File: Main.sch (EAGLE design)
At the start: 41 parts, among them IC1 LM35CZ, Q1 IRLZ44N, T1 2N3904, U1 PIC18F45K22-I/P, X1 22-23-2021

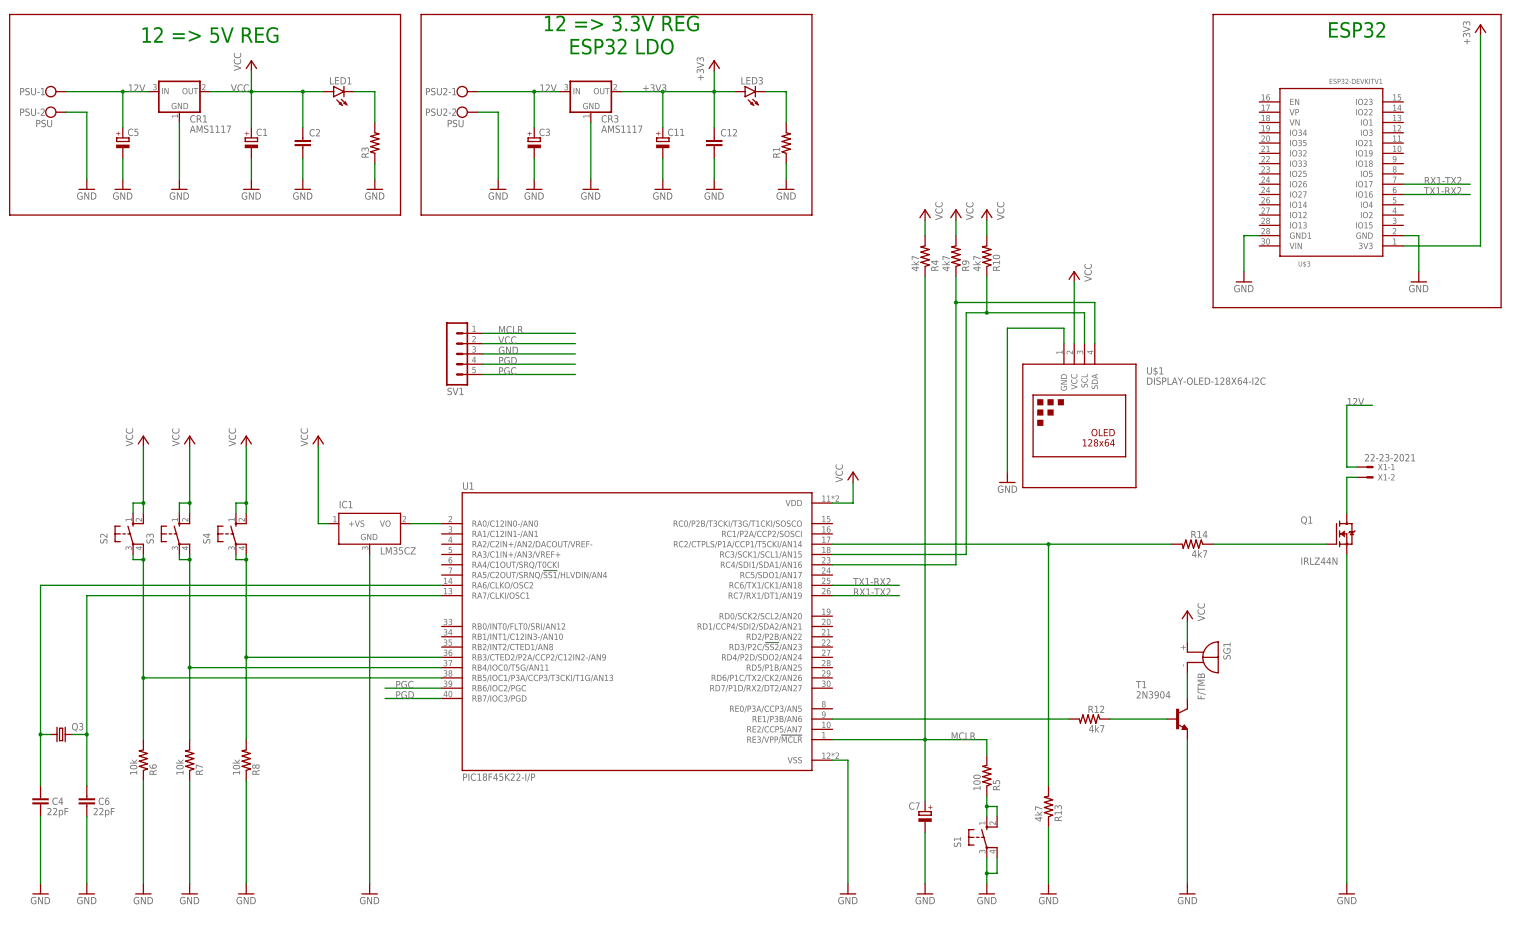
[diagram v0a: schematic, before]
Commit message: Schematic Rearranged
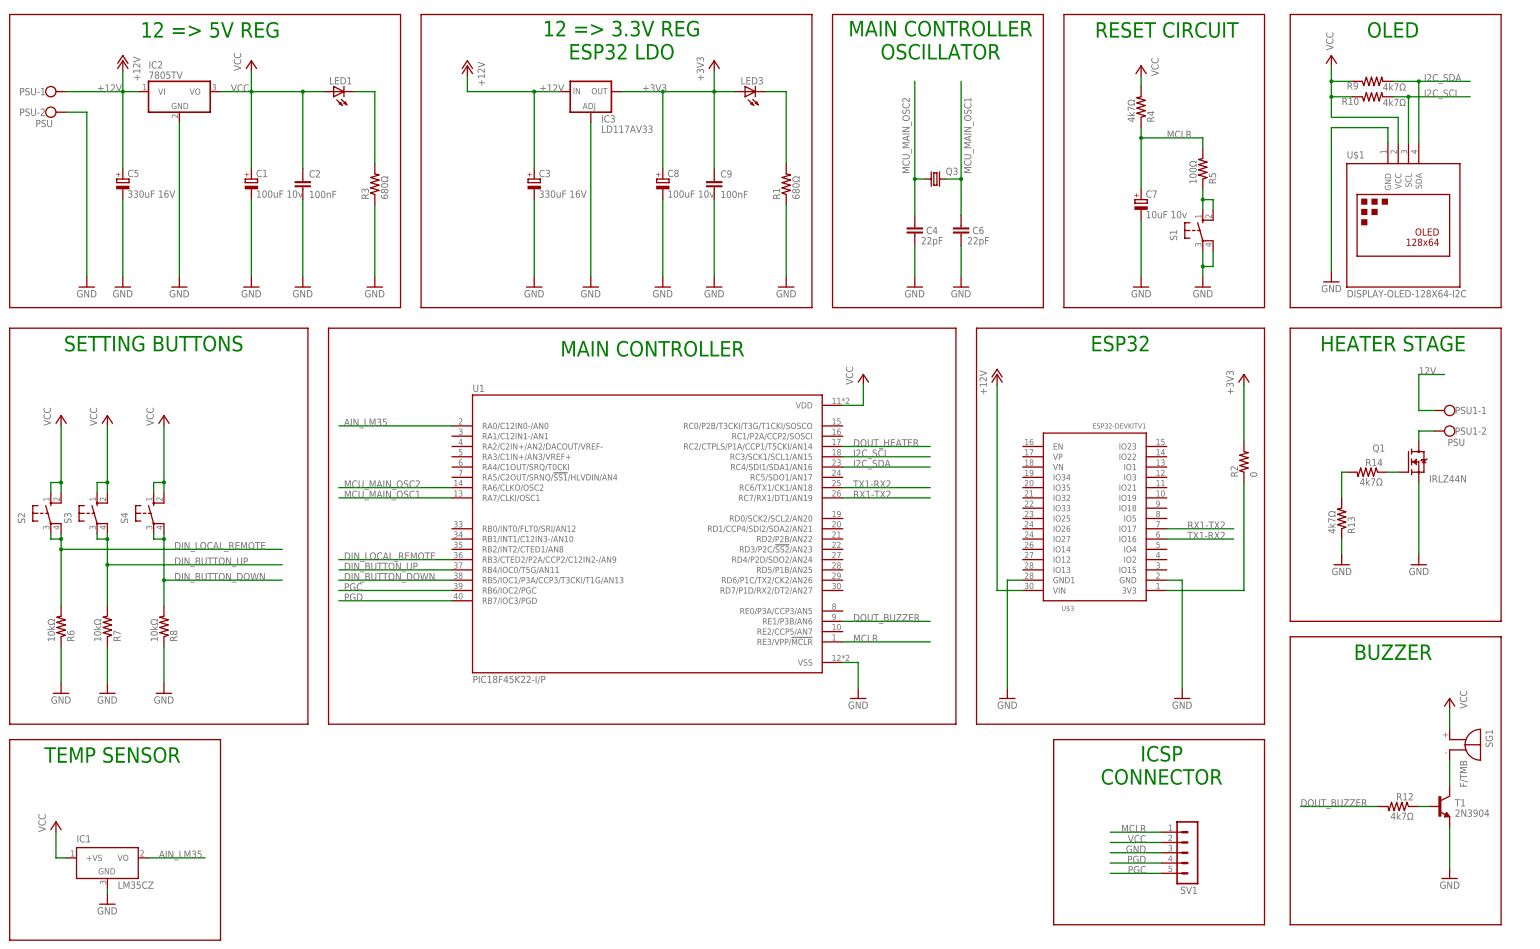
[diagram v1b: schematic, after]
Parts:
- removed C11: (no value), resistor:CPOL-EU153CLV-0505
- removed C12: (no value), resistor:C-EUC0805
- removed CR1, CR3: AMS1117, AMS1117:AMS1117
- removed PSU2: PSU, con-wago-500:W237-102
- removed X1: 22-23-2021, con-molex:22-23-2021
- added C8: 100uF 10v, resistor:CPOL-EUE2-5
- added C9: 100nF, resistor:C-EU025-060X050
- added IC2: 7805TV, linear:7805TV
- added IC3: LD117AV33, v-reg:LD117AV33
- added PSU1: PSU, con-wago-500:W237-102
- added R2: 0, resistor:R-US_0204/7
- C1: value (none) -> 100uF 10v; device resistor:CPOL-EU153CLV-0505 -> resistor:CPOL-EUE2-5
- C2: value (none) -> 100nF; device resistor:C-EUC0805 -> resistor:C-EU025-060X050
- C3, C5: value (none) -> 330uF 16V; device resistor:CPOL-EU153CLV-0505 -> resistor:CPOL-EUE2-5
- C4, C6: device resistor:C-EUC0805 -> resistor:C-EU025-024X044
- C7: value (none) -> 10uF 10v; device resistor:CPOL-EU153CLV-0505 -> resistor:CPOL-EUE2-5
- LED1, LED3: device led:LEDSML0805 -> led:LED5MM
- R1, R3: value (none) -> 680Ω
- R10, R12, R13, R14, R4, R9: value 4k7 -> 4k7Ω
- R5: value 100 -> 100Ω
- R6, R7, R8: value 10k -> 10kΩ
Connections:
- net MCU_XI2 renamed MCU_MAIN_OSC2
- net MCU_XO2 renamed MCU_MAIN_OSC1
- net N$19 renamed DOUT_BUZZER
- net N$20 renamed AIN_LM35
- net N$7 renamed DIN_BUTTON_UP
- removed net N$17: R10.1, U$1.SCL, U1.RC3/SCK1/SCL1/AN15
- removed net N$18: R9.1, U$1.SDA, U1.RC4/SDI1/SDA1/AN16
- removed net N$5: R8.2, S4.P, S4.P1, U1.RB3/CTED2/P2A/CCP2/C12IN2-/AN9
- removed net N$8: R6.2, S2.P, S2.P1, U1.RB5/IOC1/P3A/CCP3/T3CKI/T1G/AN13
- new net +12V: C3.+, C5.+, IC2.VI, IC3.IN, PSU-1.KL, U$3.VIN
- new net DIN_BUTTON_DOWN: R8.2, S4.P, S4.P1, U1.RB5/IOC1/P3A/CCP3/T3CKI/T1G/AN13
- new net DIN_LOCAL_REMOTE: R6.2, S2.P, S2.P1, U1.RB3/CTED2/P2A/CCP2/C12IN2-/AN9
- new net DOUT_HEATER: U1.RC2/CTPLS/P1A/CCP1/T5CKI/AN14
- new net I2C_SCL: R10.2, U$1.SCL, U1.RC3/SCK1/SCL1/AN15
- new net I2C_SDA: R9.2, U$1.SDA, U1.RC4/SDI1/SDA1/AN16
- new net N$2: R2.1, U$3.3V3
- net +3V3: now also C8.+, C9.1, IC3.OUT, R2.2; no longer C11.+, C12.1, CR3.OUT, U$3.3V3
- net 12V: now also PSU1-1.KL; no longer C3.+, C5.+, CR1.IN, CR3.IN, PSU-1.KL, PSU2-1.KL, X1-1.S
- net GND: now also C8.-, C9.2, IC2.GND, IC3.ADJ; no longer C11.-, C12.2, CR1.GROUND, CR3.GROUND, PSU2-2.KL
- net N$27: no longer U1.RC2/CTPLS/P1A/CCP1/T5CKI/AN14
- net N$29: now also PSU1-2.KL; no longer X1-2.S
- net VCC: now also IC2.VO, R10.1, R9.1; no longer CR1.OUT, R10.2, R9.2
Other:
- note added: "BUZZER"
- note added: "HEATER STAGE"
- note added: "ICSP CONNECTOR"
- note added: "MAIN CONTROLLER"
- note added: "MAIN CONTROLLER OSCILLATOR"
- note added: "OLED"
- note added: "RESET CIRCUIT"
- note added: "SETTING BUTTONS"
- note added: "TEMP SENSOR"
- moved on the sheet: C1, C2, C3, C4, C5, C6, C7, IC1, Q1, Q3, R1, R10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

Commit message: Renamed Resistors and capacitors
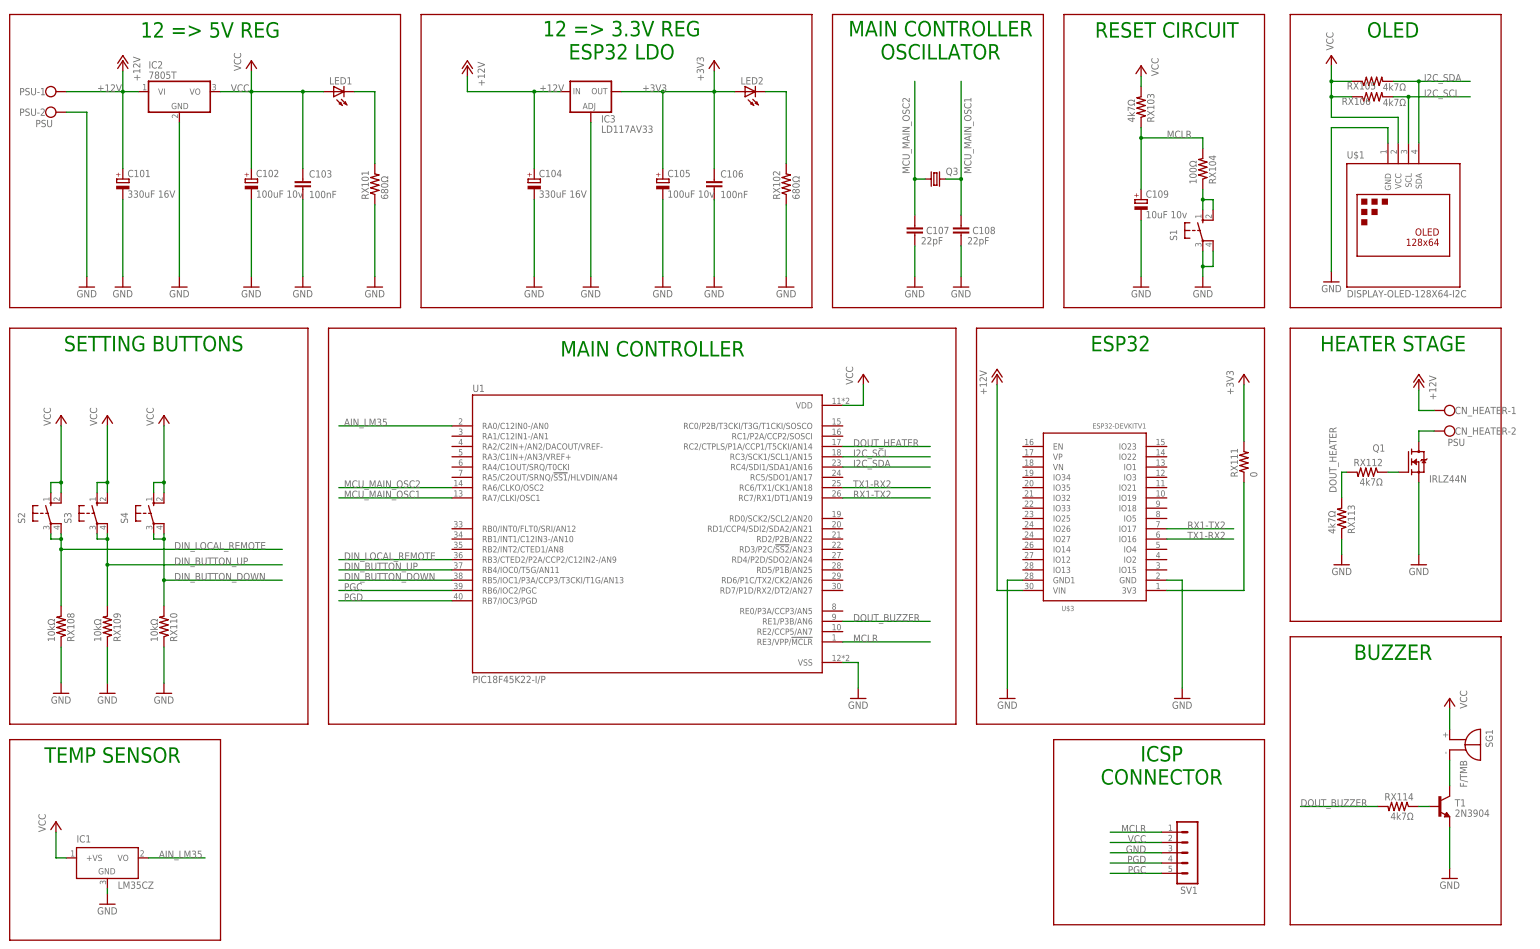
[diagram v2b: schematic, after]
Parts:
- IC2: value 7805TV -> 7805T; device linear:7805TV -> adafruit:7805T
- renumbered C1 to C102, C2 to C103, C3 to C104, C4 to C107, C5 to C101, C6 to C108, C7 to C109, C8 to C105, C9 to C106, LED3 to LED2, PSU1 to CN_HEATER, R1 to RX102, R10 to RX106, R12 to RX114, R13 to RX113, R14 to RX112, R2 to RX111, R3 to RX101, R4 to RX103, R5 to RX104, R6 to RX108, R7 to RX109, R8 to RX110, R9 to RX105
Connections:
- removed net 12V: CN_HEATER-1.KL
- removed net N$27: RX112.2, RX113.2
- net +12V: now also CN_HEATER-1.KL
- net DOUT_HEATER: now also RX112.2, RX113.2

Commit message: Components placed, Previous to start routing
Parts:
- IC1: value LM35CZ -> 7805T; device lm35:LM35CZ -> adafruit:7805T
- IC2: value 7805T -> LD117AV33; device adafruit:7805T -> v-reg:LD117AV33
- IC3: value LD117AV33 -> LM35CZ; device v-reg:LD117AV33 -> lm35:LM35CZ
- renumbered C101 to C1, C102 to C2, C103 to C3, C104 to C4, C105 to C5, C106 to C6, C107 to C7, C108 to C8, C109 to C9, RX101 to R1, RX102 to R2, RX103 to R3, RX104 to R4, RX105 to R5, RX106 to R6, RX108 to R8, RX109 to R9, RX110 to R10, RX111 to R11, RX112 to R12, RX113 to R13, RX114 to R14
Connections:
- net +12V: now also IC1.VI, IC2.IN; no longer IC2.VI, IC3.IN
- net +3V3: now also IC2.OUT; no longer IC3.OUT
- net AIN_LM35: now also IC3.VO; no longer IC1.VO
- net GND: now also IC2.ADJ, IC3.GND; no longer IC2.GND, IC3.ADJ
- net VCC: now also IC1.VO, IC3.+VS; no longer IC1.+VS, IC2.VO

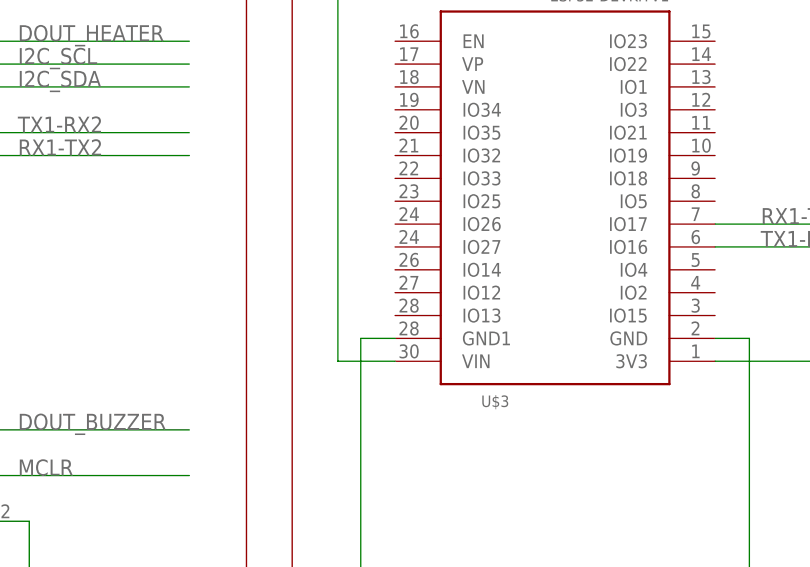
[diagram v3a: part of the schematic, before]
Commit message: Routing. I2C lines Pending
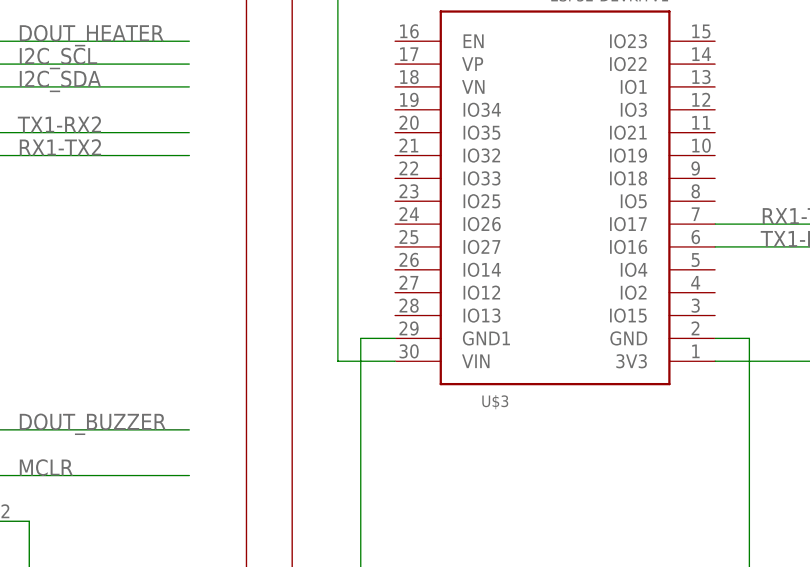
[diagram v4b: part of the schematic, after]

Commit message: Ready to deliver
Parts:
- CN_HEATER: value PSU -> HEATER
- Q3: value (none) -> 20MHz
- S2: value (none) -> LOCAL/REMOTE
- S3: value (none) -> UP
- S4: value (none) -> DOWN
- renumbered SG1 to BUZZER
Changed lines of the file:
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@@
 <part name="R4" library="resistor" deviceset="R-US_" device="0204/7" value="100Ω"/>
 <part name="GND10" library="supply1" library_urn="urn:adsk.eagle:library:371" deviceset="GND" device=""/>
-<part name="Q3" library="crystal" deviceset="CRYSTAL" device="HC49S"/>
+<part name="Q3" library="crystal" deviceset="CRYSTAL" device="HC49S" value="20MHz"/>
 <part name="S1" library="switch-omron" library_urn="urn:adsk.eagle:library:377" deviceset="10-XX" device="" package3d_urn="urn:adsk.eagle:package:27496/1"/>
-<part name="S2" library="switch-omron" library_urn="urn:adsk.eagle:library:377" deviceset="10-XX" device="" package3d_urn="urn:adsk.eagle:package:27496/1"/>
-<part name="S3" library="switch-omron" library_urn="urn:adsk.eagle:library:377" deviceset="10-XX" device="" package3d_urn="urn:adsk.eagle:package:27496/1"/>
-<part name="S4" library="switch-omron" library_urn="urn:adsk.eagle:library:377" deviceset="10-XX" device="" package3d_urn="urn:adsk.eagle:package:27496/1"/>
+<part name="S2" library="switch-omron" library_urn="urn:adsk.eagle:library:377" deviceset="10-XX" device="" package3d_urn="urn:adsk.eagle:package:27496/1" value="LOCAL/REMOTE"/>
+<part name="S3" library="switch-omron" library_urn="urn:adsk.eagle:library:377" deviceset="10-XX" device="" package3d_urn="urn:adsk.eagle:package:27496/1" value="UP"/>
+<part name="S4" library="switch-omron" library_urn="urn:adsk.eagle:library:377" deviceset="10-XX" device="" package3d_urn="urn:adsk.eagle:package:27496/1" value="DOWN"/>
 <part name="IC3" library="lm35" deviceset="LM35" device="CZ"/>
 <part name="P+5" library="supply1" library_urn="urn:adsk.eagle:library:371" deviceset="VCC" device=""/>
@@
 <part name="R5" library="resistor" deviceset="R-US_" device="0204/7" value="4k7Ω"/>
 <part name="R6" library="resistor" deviceset="R-US_" device="0204/7" value="4k7Ω"/>
-<part name="SG1" library="buzzer" deviceset="F/TMB" device=""/>
+<part name="BUZZER" library="buzzer" deviceset="F/TMB" device=""/>
 <part name="T1" library="transistor" library_urn="urn:adsk.eagle:library:402" deviceset="2N3904" device="" package3d_urn="urn:adsk.eagle:package:28523/2"/>
 <part name="R14" library="resistor" deviceset="R-US_" device="0204/7" value="4k7Ω"/>
@@
 <part name="IC1" library="adafruit" deviceset="78*" device="T" technology="05"/>
 <part name="IC2" library="v-reg" deviceset="LD117A?*" device="V" technology="33"/>
-<part name="CN_HEATER" library="con-wago-500" library_urn="urn:adsk.eagle:library:195" deviceset="W237-102" device="" package3d_urn="urn:adsk.eagle:package:10688/1" value="PSU"/>
+<part name="CN_HEATER" library="con-wago-500" library_urn="urn:adsk.eagle:library:195" deviceset="W237-102" device="" package3d_urn="urn:adsk.eagle:package:10688/1" value="HEATER"/>
 <part name="P+9" library="supply1" library_urn="urn:adsk.eagle:library:371" deviceset="+12V" device=""/>
 <part name="P+11" library="supply1" library_urn="urn:adsk.eagle:library:371" deviceset="+12V" device=""/>
@@
 <attribute name="VALUE" x="347.98" y="231.902" size="1.778" layer="96" rot="MR180"/>
 </instance>
-<instance part="SG1" gate="1" x="367.03" y="73.66" smashed="yes" rot="R270">
+<instance part="BUZZER" gate="1" x="367.03" y="73.66" smashed="yes" rot="R270">
 <attribute name="NAME" x="373.38" y="76.2" size="1.778" layer="95" rot="R270"/>
 <attribute name="VALUE" x="367.03" y="68.58" size="1.778" layer="96" rot="R270"/>
@@
 <segment>
 <pinref part="P+14" gate="VCC" pin="VCC"/>
-<pinref part="SG1" gate="1" pin="+"/>
+<pinref part="BUZZER" gate="1" pin="+"/>
 <wire x1="364.49" y1="81.28" x2="364.49" y2="76.2" width="0.1524" layer="91"/>
 </segment>
@@
 <net name="N$26" class="0">
 <segment>
-<pinref part="SG1" gate="1" pin="-"/>
+<pinref part="BUZZER" gate="1" pin="-"/>
 <wire x1="364.49" y1="68.58" x2="364.49" y2="62.23" width="0.1524" layer="91"/>
 <pinref part="T1" gate="G1" pin="C"/>

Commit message: Ready to deliver
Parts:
- S1: value (none) -> RESET
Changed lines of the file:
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@@
 <part name="GND10" library="supply1" library_urn="urn:adsk.eagle:library:371" deviceset="GND" device=""/>
 <part name="Q3" library="crystal" deviceset="CRYSTAL" device="HC49S" value="20MHz"/>
-<part name="S1" library="switch-omron" library_urn="urn:adsk.eagle:library:377" deviceset="10-XX" device="" package3d_urn="urn:adsk.eagle:package:27496/1"/>
+<part name="S1" library="switch-omron" library_urn="urn:adsk.eagle:library:377" deviceset="10-XX" device="" package3d_urn="urn:adsk.eagle:package:27496/1" value="RESET"/>
 <part name="S2" library="switch-omron" library_urn="urn:adsk.eagle:library:377" deviceset="10-XX" device="" package3d_urn="urn:adsk.eagle:package:27496/1" value="LOCAL/REMOTE"/>
 <part name="S3" library="switch-omron" library_urn="urn:adsk.eagle:library:377" deviceset="10-XX" device="" package3d_urn="urn:adsk.eagle:package:27496/1" value="UP"/>
@@
 <instance part="S1" gate="1" x="303.53" y="199.39" smashed="yes">
 <attribute name="NAME" x="297.18" y="196.85" size="1.778" layer="95" rot="R90"/>
-<attribute name="VALUE" x="299.72" y="202.565" size="1.778" layer="96" rot="R90"/>
+<attribute name="VALUE" x="309.88" y="194.945" size="1.778" layer="96" rot="R90"/>
 </instance>
 <instance part="S2" gate="1" x="19.05" y="129.54" smashed="yes">
